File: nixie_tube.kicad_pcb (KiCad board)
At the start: 2 copper layers, 26.2 x 48 mm, 22 parts, among them J1 Conn_01x06_Male, J11 dc003a, J2 Conn_01x06_Female, J3 Conn_01x01_Male, J4 Conn_01x01_Female, Q1 SS8550, Q2 FQD5N60C, Q3 Q_NPN_BCE, Q4 AO3400, U1 MC34063

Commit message: add extra mlcc footprint in cp radial fp
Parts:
- moved J3 2.30 mm to (177.7, 83.2)
- moved J4 2.30 mm to (191.2, 83.2)
- moved R2 0.10 mm to (171.9, 120.8)
- moved J2 0.10 mm to (177.6, 125.5)
- moved Q1 0.10 mm to (174.8, 120.8)
- moved R5 0.10 mm to (175.6, 124.0)
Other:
- board size 26.2 x 48 mm -> 26.2 x 53.3 mm
- board text removed: "26.5x48mm"

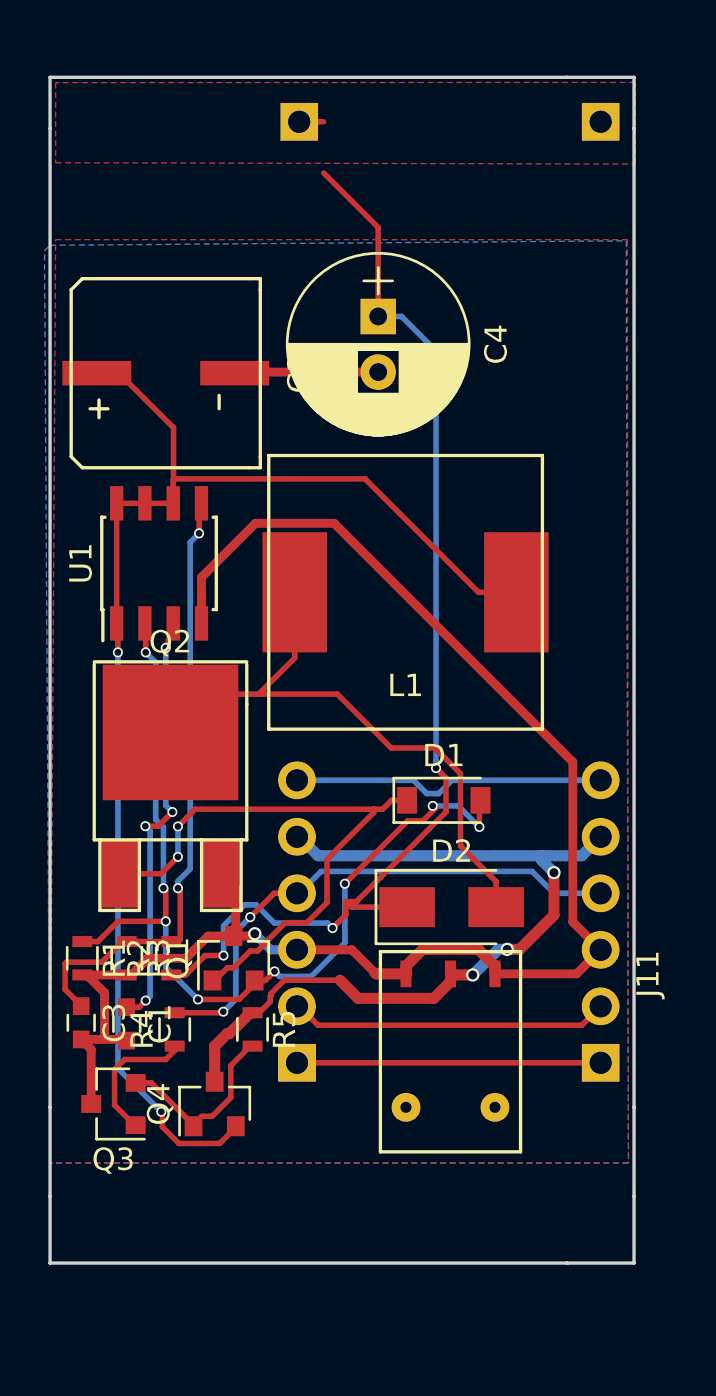
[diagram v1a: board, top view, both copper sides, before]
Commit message: reallocate space for 4 m3 pins
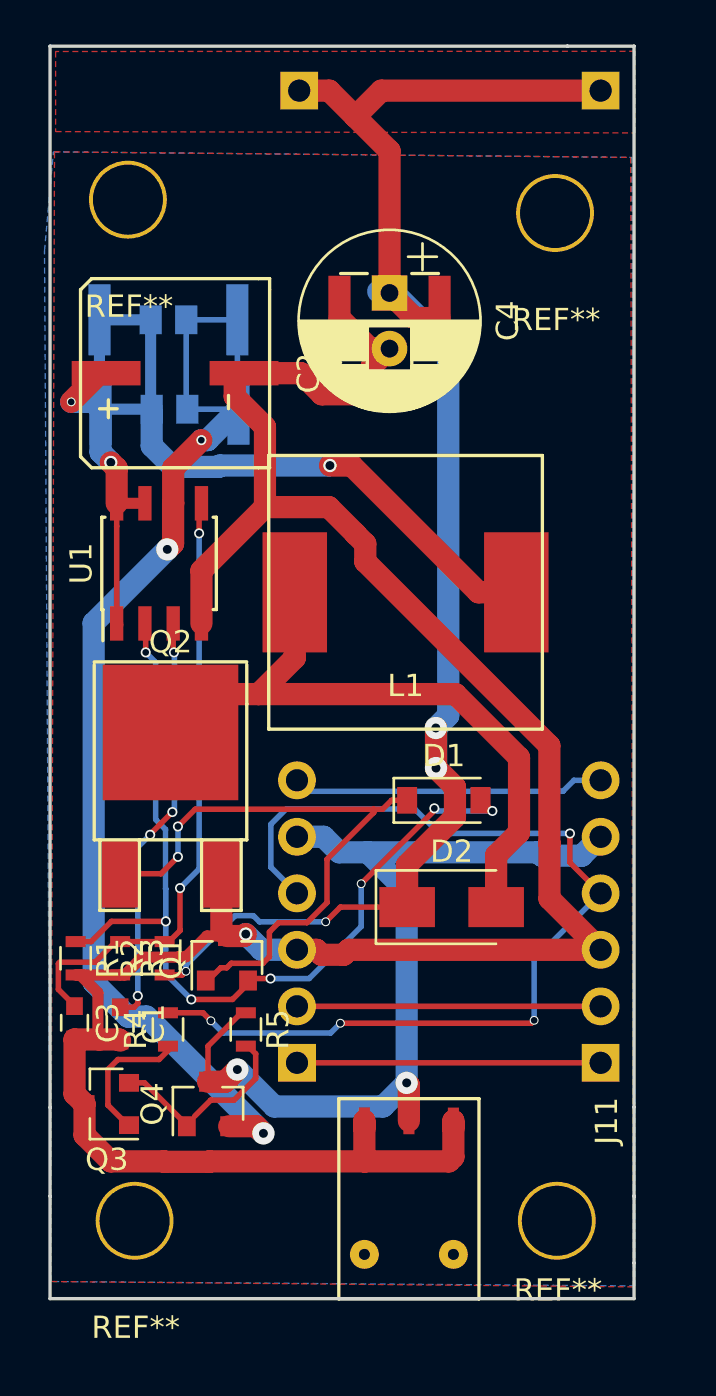
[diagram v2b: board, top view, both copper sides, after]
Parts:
- added R6: R, nixie-tube-fp:R_2512_0805, B.Cu at (171.9, 96.1)
- added R7: R, nixie-tube-fp:R_2512_0805, B.Cu at (171.8, 92.1)
- added REF**: mountingHole, nixie-tube-fp:mountingHole, F.Cu at (170.0, 86.7)
- added REF**: mountingHole, nixie-tube-fp:mountingHole, F.Cu at (189.2, 87.3)
- added REF**: mountingHole, nixie-tube-fp:mountingHole, F.Cu at (170.3, 132.6)
- added REF**: mountingHole, nixie-tube-fp:mountingHole, F.Cu at (189.3, 130.9)
- C4: footprint Capacitors_THT:CP_Radial_D8.0mm_P2.50mm -> nixie-tube-fp:CP_RADIAL_and_mlcc
- Q4: value AO3400 -> AO3407
- moved J11 6.87 mm to (184.6, 134.1)
- moved J3 1.40 mm to (177.7, 81.8)
- moved J4 1.40 mm to (191.2, 81.8)
- moved C4 0.51 mm to (181.8, 92.0)
- moved C2 0.42 mm to (172.1, 94.5)
- moved C3 0.30 mm to (167.6, 123.7)
- moved Q1 0.30 mm to (174.4, 120.8)
- moved Q4 0.30 mm to (173.6, 127.3)
- moved C1 0.30 mm to (169.7, 123.8)
- moved Q3 0.30 mm to (169.1, 127.3)
- moved R1 0.30 mm to (167.7, 120.8)
- moved R2 0.30 mm to (171.7, 120.8)
- moved R3 0.30 mm to (169.7, 120.8)
- moved R4 0.30 mm to (171.8, 124.0)
- moved R5 0.30 mm to (175.3, 124.0)
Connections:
- net +9V renamed +VDC
- net /OE renamed /STORE
- Q4 pad 2: Net-(C2-Pad1) -> Net-(Q4-Pad2)
- U1 pad 6: Net-(C2-Pad1) -> Net-(Q4-Pad2)
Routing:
- net Net-(Q4-Pad2): track 0.00 -> 53.5 mm, vias 0 -> 3
- net GND: track 78.3 -> 110.6 mm
- net /PWREN: track 24.0 -> 45.1 mm, vias 2 -> 4
- net Net-(C4-Pad1): track 52.9 -> 71.0 mm, vias 3 -> 4
- net Net-(C2-Pad1): track 60.8 -> 49.0 mm, vias 2 -> 3
- net +VDC: track 37.6 -> 41.4 mm, vias 3 -> 2
- net Net-(D2-Pad2): track 27.1 -> 30.0 mm
- net Net-(D1-Pad1): track 26.7 -> 27.6 mm
- net Net-(D1-Pad2): track 42.3 -> 41.6 mm, vias 8 -> 7
- net /SCK: track 14.3 -> 13.7 mm
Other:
- board size 26.2 x 53.3 mm -> 26.2 x 56.3 mm
- net class GND: trace_width 0.4 -> 1
- net class HV added: clearance 0.2, trace_width 1, via_dia 1, via_drill 0.4
- board text removed: "mlcc"

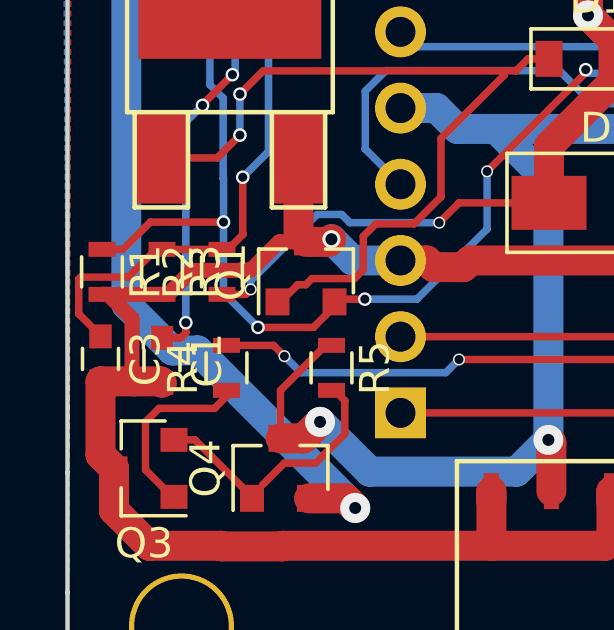
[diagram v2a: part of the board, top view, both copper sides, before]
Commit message: move component away from each other, require rerout for some of them :|
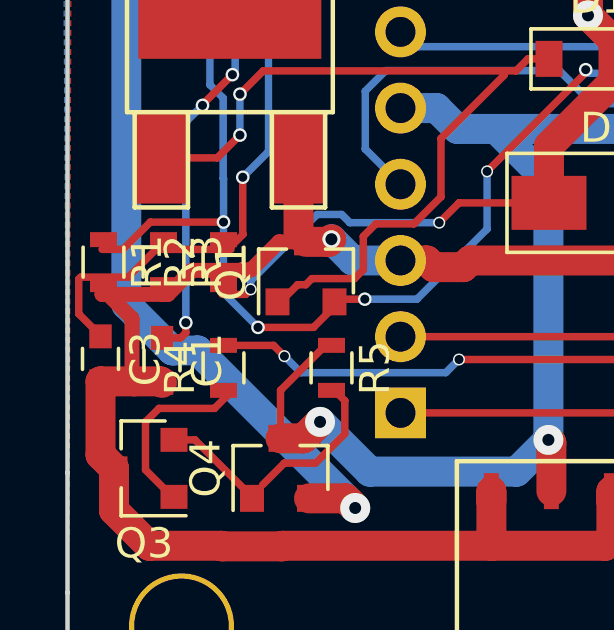
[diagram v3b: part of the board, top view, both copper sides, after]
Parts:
- moved R1 0.33 mm to (167.7, 120.5)
- moved R2 0.33 mm to (171.7, 120.5)
- moved R3 0.33 mm to (169.7, 120.5)
- moved R4 0.10 mm to (171.7, 124.0)
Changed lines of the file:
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@@
     (area 166.424999 79.724999 192.825001 136.175001)
     (thickness 1.6)
-    (drawings 12)
+    (drawings 13)
     (tracks 325)
     (zones 0)
@@
   (page A4)
   (layers
-    (0 F.Cu signal)
-    (31 B.Cu signal)
+    (0 F.Cu signal hide)
+    (31 B.Cu signal hide)
     (32 B.Adhes user)
     (33 F.Adhes user)
@@
   )
   (module Resistors_SMD:R_0603 locked (layer F.Cu)
-    (at 171.8 124 90)
+    (at 171.7 124 90)
     (descr "Resistor SMD 0603, reflow soldering, Vishay (see dcrcw.pdf)")
     (tags "resistor 0603")
@@
   )
   (module Resistors_SMD:R_0603 locked (layer F.Cu)
-    (at 169.65 120.8 270)
+    (at 169.7 120.475 270)
     (descr "Resistor SMD 0603, reflow soldering, Vishay (see dcrcw.pdf)")
     (tags "resistor 0603")
@@
   )
   (module Resistors_SMD:R_0603 locked (layer F.Cu)
-    (at 171.65 120.8 90)
+    (at 171.7 120.475 90)
     (descr "Resistor SMD 0603, reflow soldering, Vishay (see dcrcw.pdf)")
     (tags "resistor 0603")
@@
   )
   (module Resistors_SMD:R_0603 locked (layer F.Cu)
-    (at 167.65 120.8 270)
+    (at 167.7 120.475 270)
     (descr "Resistor SMD 0603, reflow soldering, Vishay (see dcrcw.pdf)")
     (tags "resistor 0603")
@@
     )
   )
+  (dimension 31 (width 0.3) (layer Eco1.User)
+    (gr_text "31.000 mm" (at 195.05 97.3 90) (layer Eco1.User)
+      (effects (font (size 1.5 1.5) (thickness 0.3)))
+    )
+    (feature1 (pts (xy 191.25 81.8) (xy 196.4 81.8)))
+    (feature2 (pts (xy 191.25 112.8) (xy 196.4 112.8)))
+    (crossbar (pts (xy 193.7 112.8) (xy 193.7 81.8)))
+    (arrow1a (pts (xy 193.7 81.8) (xy 194.286421 82.926504)))
+    (arrow1b (pts (xy 193.7 81.8) (xy 193.113579 82.926504)))
+    (arrow2a (pts (xy 193.7 112.8) (xy 194.286421 111.673496)))
+    (arrow2b (pts (xy 193.7 112.8) (xy 193.113579 111.673496)))
+  )
   (dimension 26.26 (width 0.3) (layer Eco1.User)

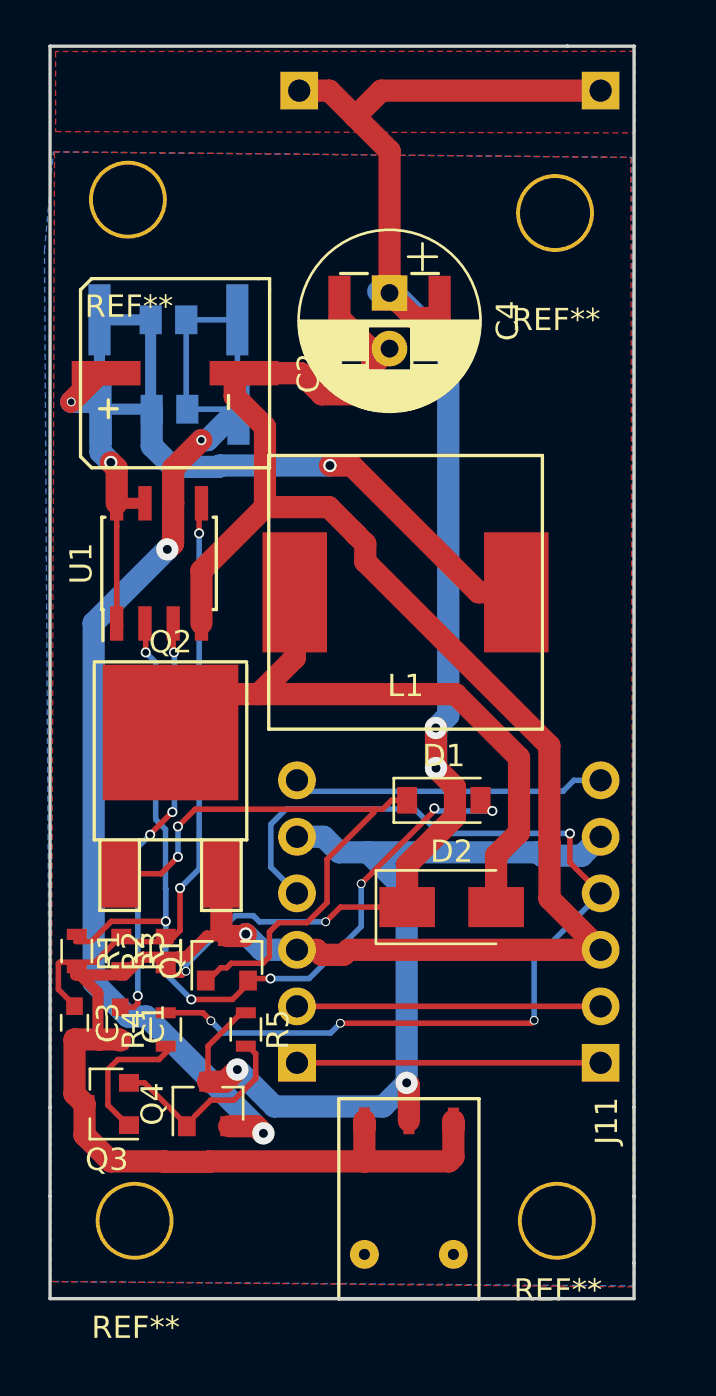
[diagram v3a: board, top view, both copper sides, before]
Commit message: routed all remaining tracks
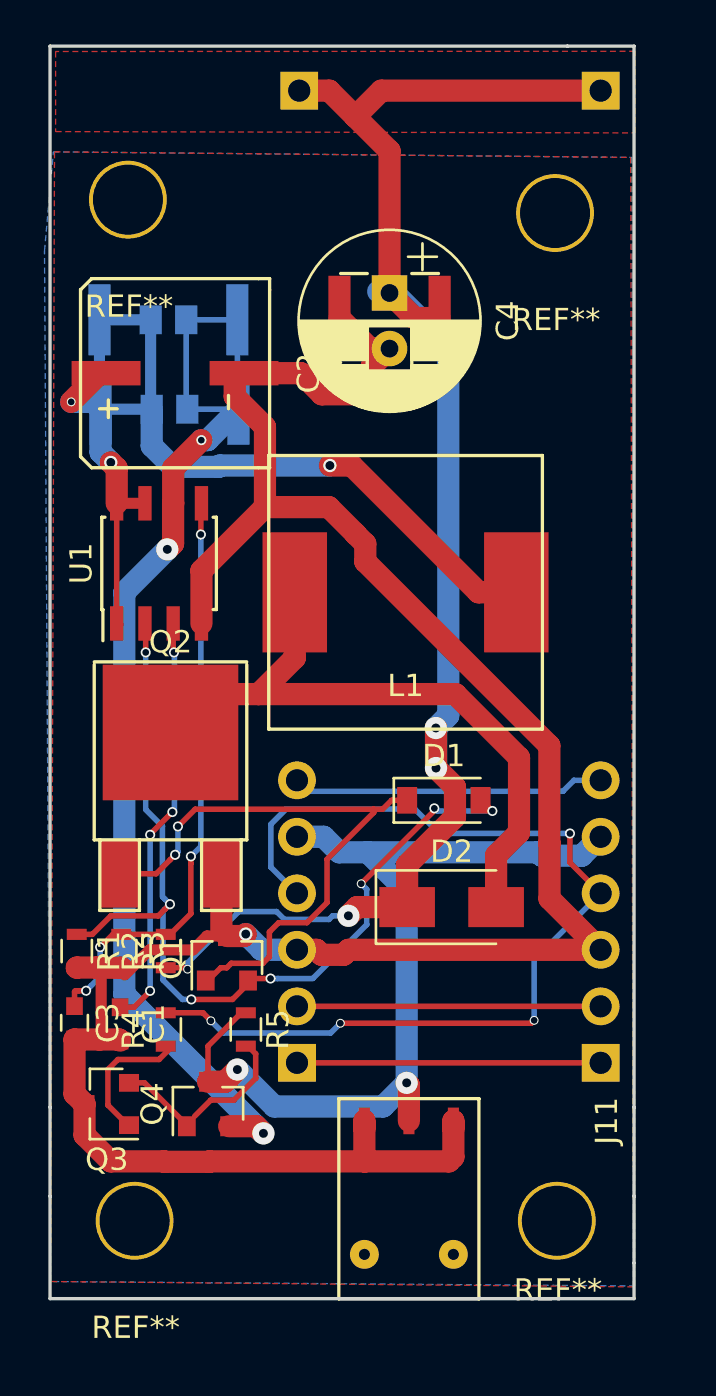
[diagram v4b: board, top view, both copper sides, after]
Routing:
- net Net-(Q4-Pad2): track 53.5 -> 51.8 mm
- net Net-(C3-Pad1): track 28.2 -> 26.9 mm, vias 2 -> 4
- net Net-(D1-Pad2): track 41.6 -> 42.7 mm
- net GND: track 110.6 -> 111.2 mm

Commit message: shrink board by .5mm in x dir
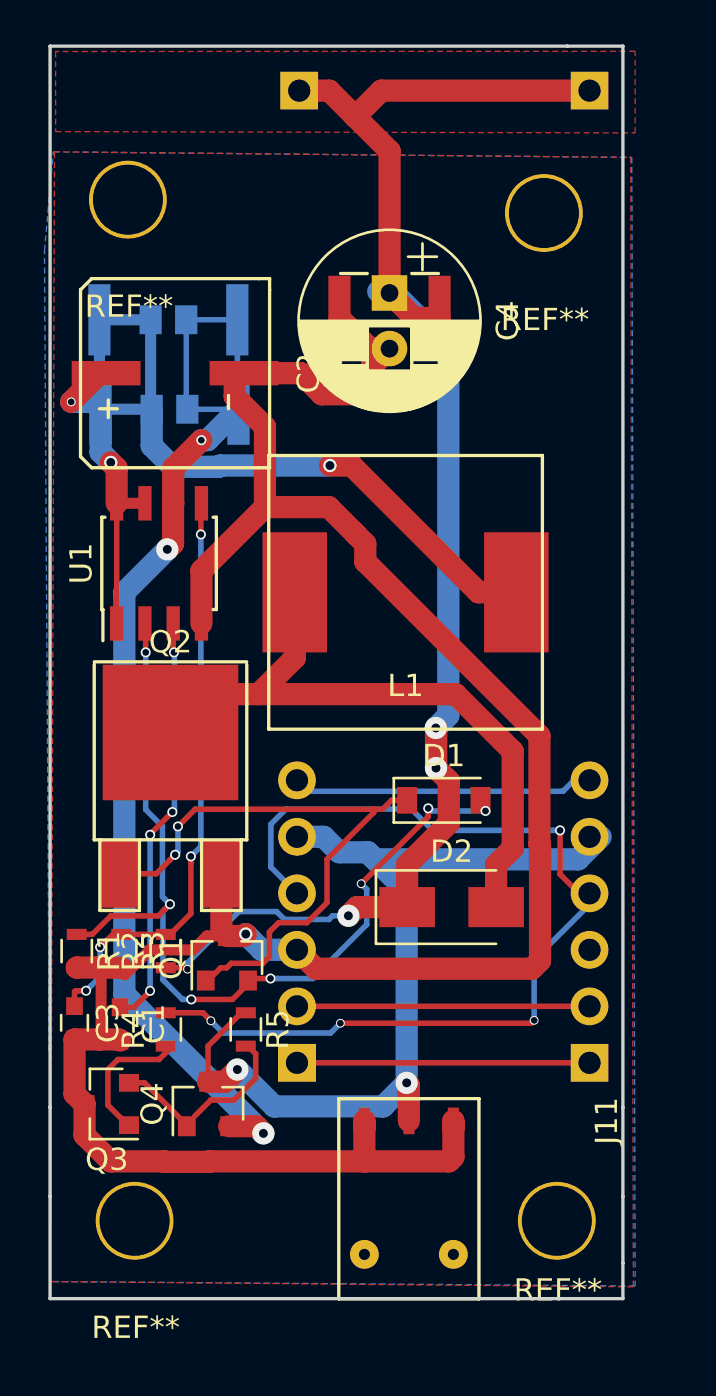
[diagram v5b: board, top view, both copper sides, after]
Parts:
- moved J1 0.50 mm to (190.8, 125.5)
- moved J4 0.50 mm to (190.8, 81.8)
- moved REF** 0.50 mm to (188.7, 87.3)
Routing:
- net GND: track 111.2 -> 108.2 mm
- net Net-(C4-Pad1): track 70.9 -> 70.2 mm
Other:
- board size 26.2 x 56.3 mm -> 25.8 x 56.3 mm

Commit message: change m3 pins to no net
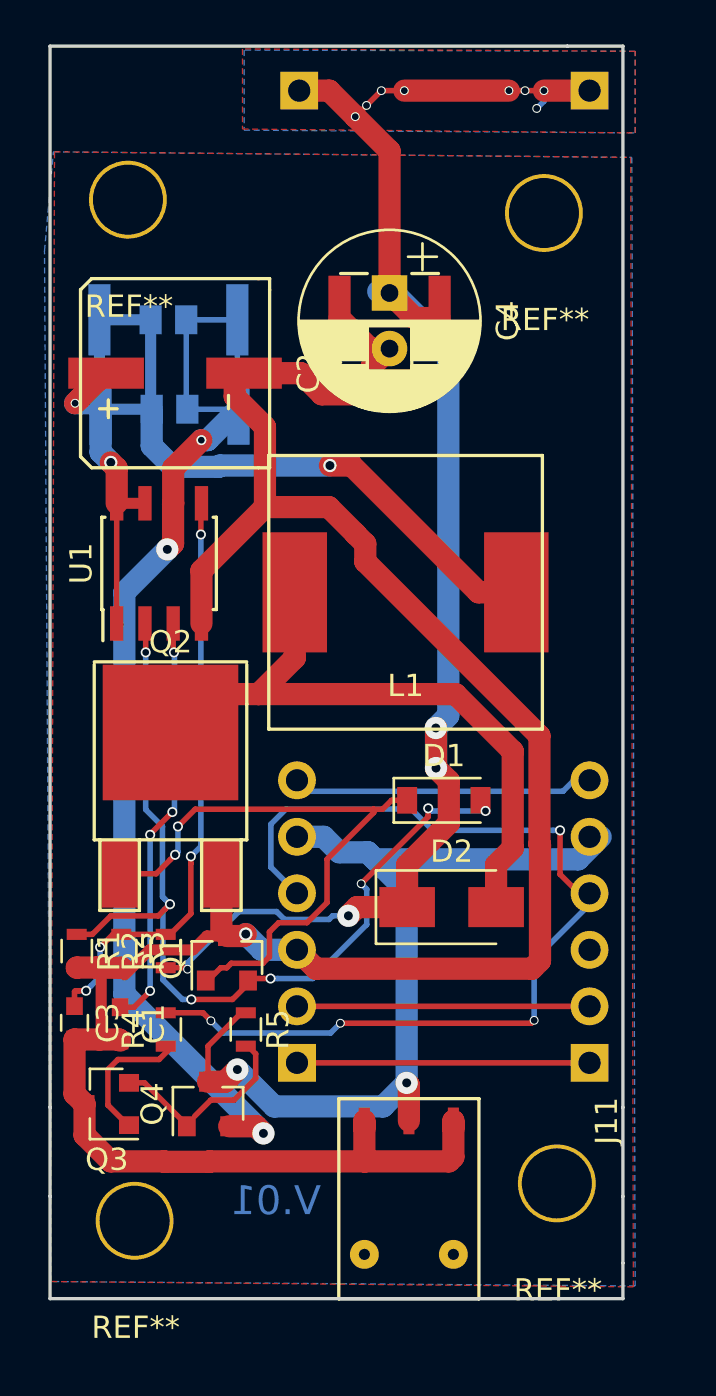
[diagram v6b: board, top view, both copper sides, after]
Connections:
- REF** pad 1: GND -> (no net) (x4)
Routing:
- net Net-(C4-Pad1): track 70.2 -> 71.1 mm, vias 4 -> 12
- added copper zone on B.Cu, net Net-(C4-Pad1)
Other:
- board text added: "V.01"

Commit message: fixed pin number not same with actual numbering of component
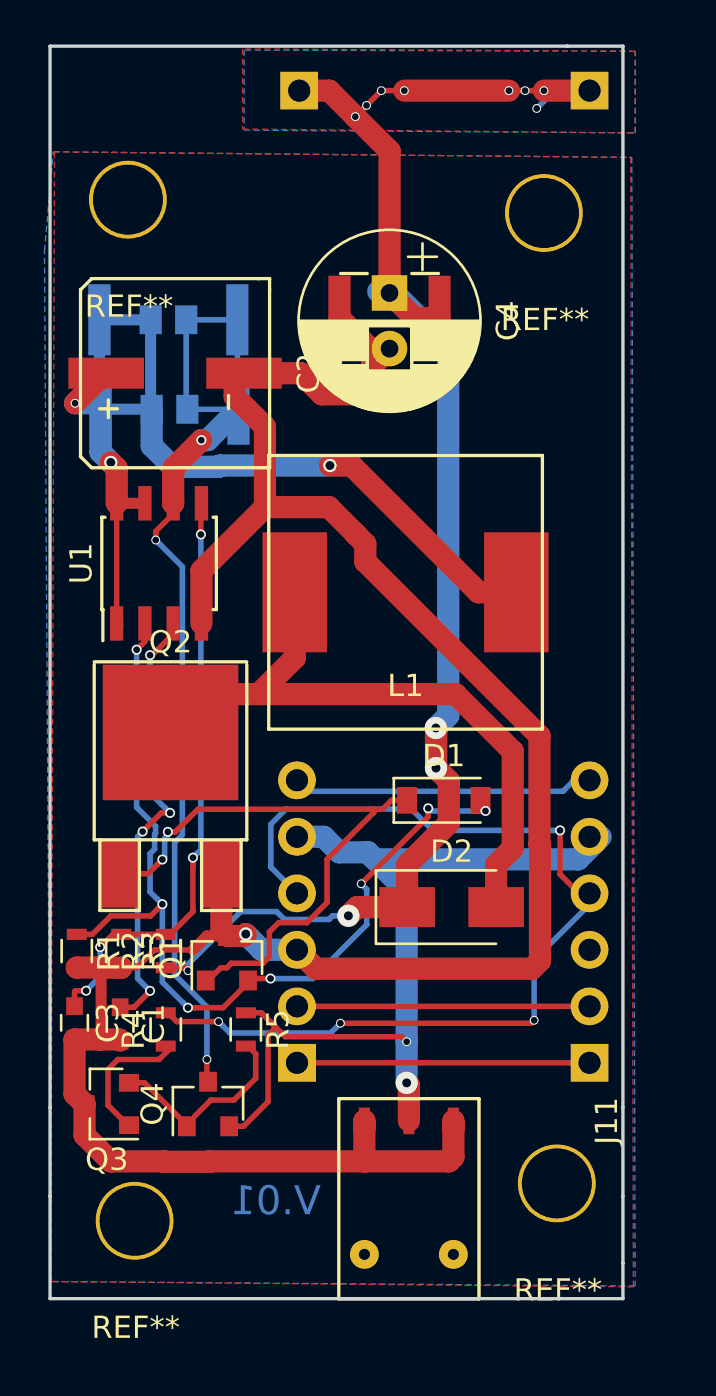
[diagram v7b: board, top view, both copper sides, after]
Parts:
- C1: value 20nF -> 10nF
- D2: value RS2M -> RS1M
- Q4: value AO3407 -> TP0610T
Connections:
- Q4 pad 2: Net-(Q4-Pad2) -> +VDC
- Q4 pad 3: +VDC -> Net-(Q4-Pad3)
- R6 pad 2: Net-(Q4-Pad2) -> Net-(Q4-Pad3)
- R7 pad 2: Net-(Q4-Pad2) -> Net-(Q4-Pad3)
- U1 pad 6: Net-(Q4-Pad2) -> Net-(Q4-Pad3)
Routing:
- net Net-(Q4-Pad2): track 51.8 -> 0.00 mm, vias 3 -> 0
- net Net-(Q4-Pad3): track 0.00 -> 45.9 mm, vias 0 -> 3
- net Net-(C1-Pad1): track 18.6 -> 20.1 mm
